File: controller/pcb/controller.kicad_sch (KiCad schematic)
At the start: 28 parts, among them J1 Conn_01x10_Pin, SW1 SW_Push, SW2 SW_Push, SW3 SW_Push, SW4 SW_Push, U1 COM-09032, U2 COM-09032, U3 NRF24L01_Breakout, U4 ESP32C3-SUPERMINI, U5 74HC148

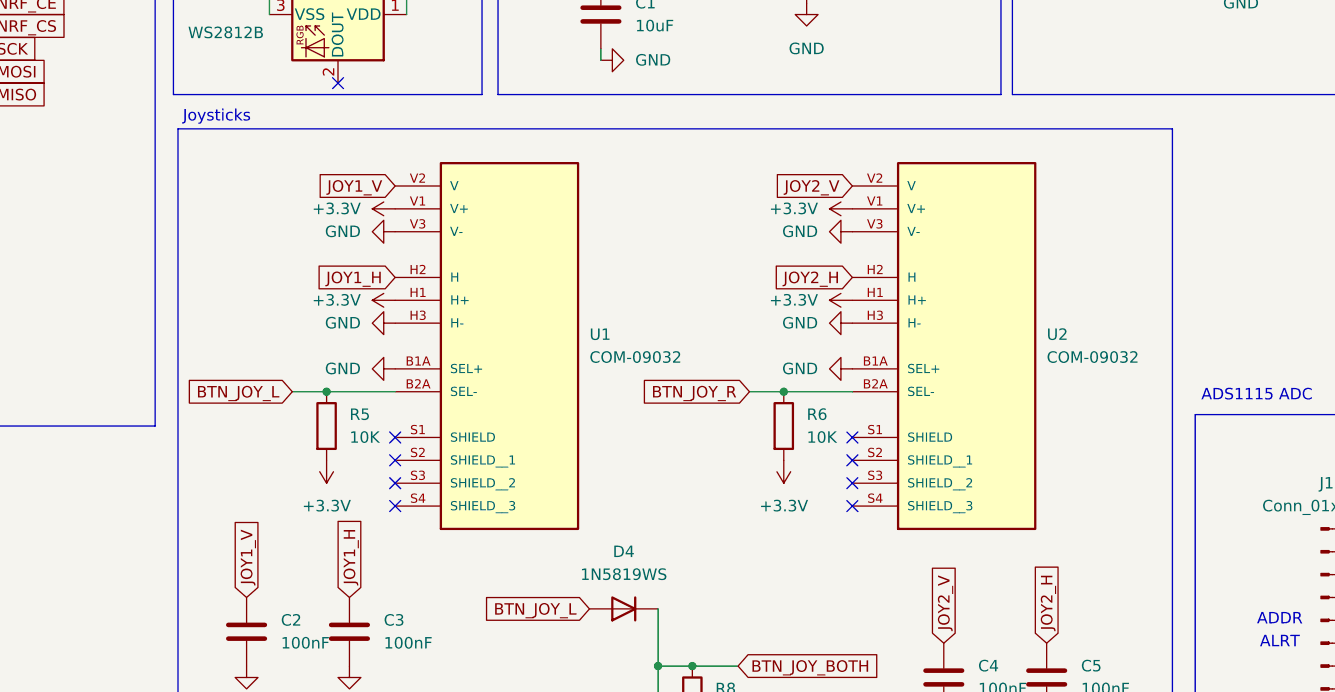
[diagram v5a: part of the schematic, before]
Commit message: [pcb] change footprint for joystick on controller
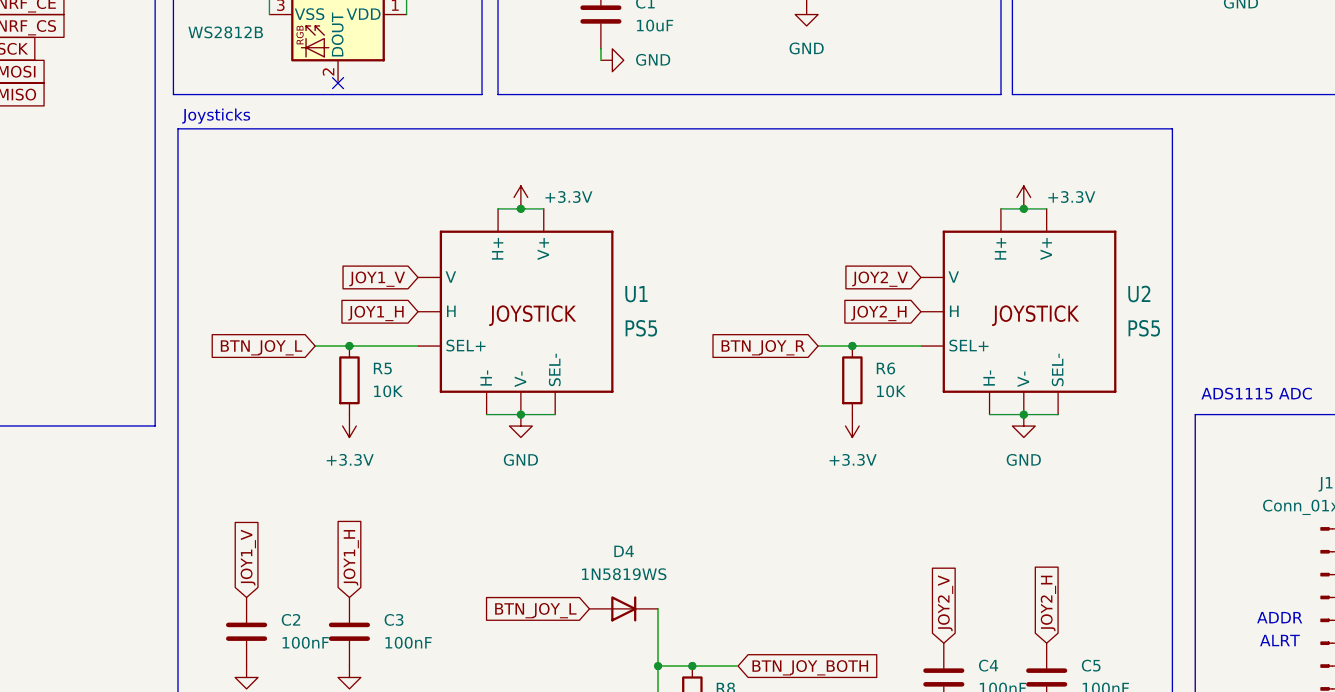
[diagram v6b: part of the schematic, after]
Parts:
- removed U1, U2: COM-09032, stuff:XDCR_COM-09032, symbol stuff:COM-09032
- added U1, U2: PS5, stuff:Joystick, symbol stuff:Joystick
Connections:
- net +3.3V: now also U1.3 (H+), U1.3' (V+), U2.3 (H+), U2.3' (V+)
- net BTN_JOY_L: now also U1.a (SEL+)
- net BTN_JOY_R: now also U2.a (SEL+)
- net GND: now also U1.1 (H-), U1.1' (V-), U1.c (SEL-), U2.1 (H-), U2.1' (V-), U2.c (SEL-)
- net JOY1_H: now also U1.2 (H)
- net JOY1_V: now also U1.2' (V)
- net JOY2_H: now also U2.2 (H)
- net JOY2_V: now also U2.2' (V)
- no-connect marks 14 -> 6
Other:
- moved on the sheet: R5, R6

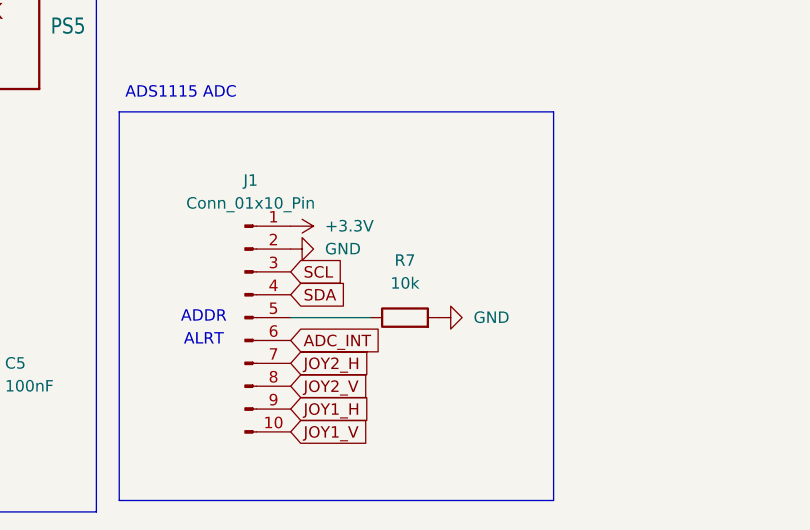
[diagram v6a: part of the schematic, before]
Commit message: [docs] add controller photos and "why" to readme
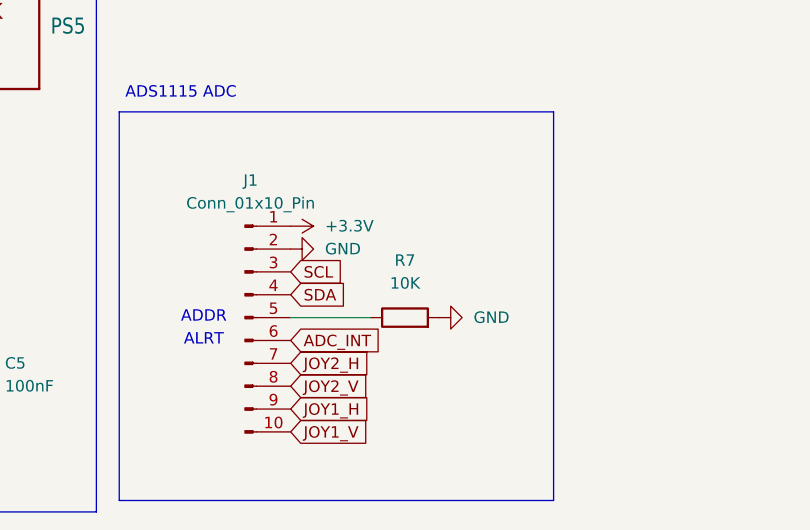
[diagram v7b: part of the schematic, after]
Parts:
- R7: value 10k -> 10K
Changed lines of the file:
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@@
 			)
 		)
-		(property "Value" "10k"
+		(property "Value" "10K"
 			(at 227.33 125.73 90)
 			(effects
